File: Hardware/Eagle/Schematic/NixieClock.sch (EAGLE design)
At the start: 10 parts

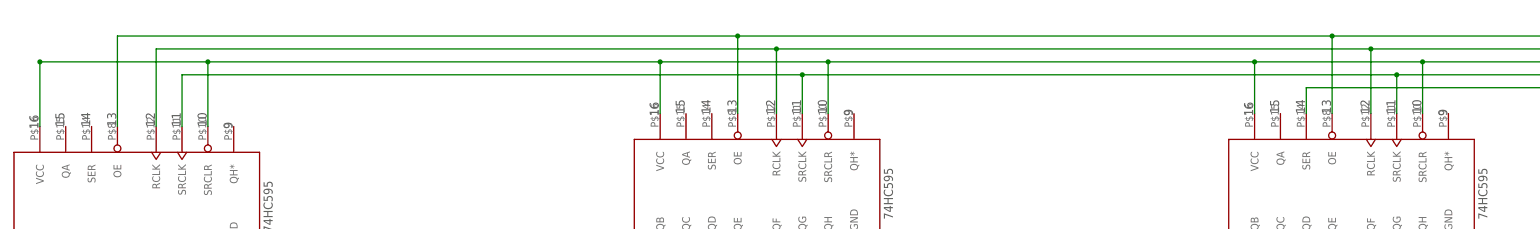
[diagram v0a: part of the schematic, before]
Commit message: Schematic progress... chips in board layout are out of order.. fix later
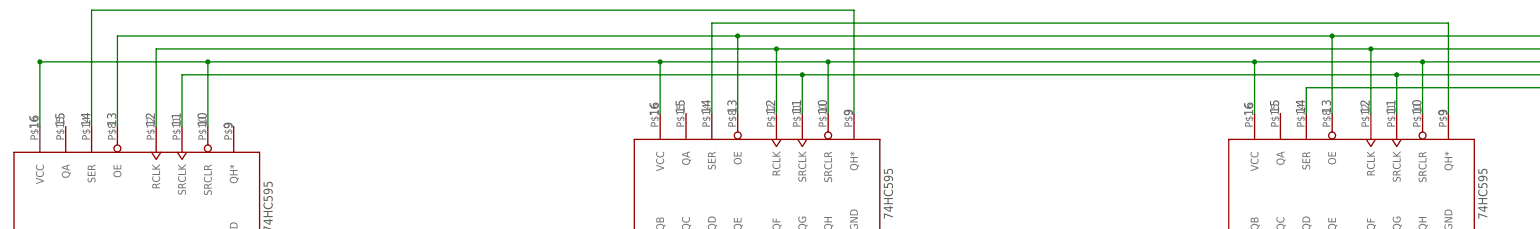
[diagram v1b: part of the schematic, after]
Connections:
- new net N$7: U$2.QH*, U$3.SER
- new net N$9: U$3.QH*, U$4.SER
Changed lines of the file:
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@@
+</segment>
+</net>
+<net name="N$7" class="0">
+<segment>
+<pinref part="U$2" gate="G$1" pin="QH*"/>
+<wire x1="124.46" y1="48.26" x2="124.46" y2="66.04" width="0.1524" layer="91"/>
+<pinref part="U$3" gate="G$1" pin="SER"/>
+<wire x1="124.46" y1="66.04" x2="-20.32" y2="66.04" width="0.1524" layer="91"/>
+<wire x1="-20.32" y1="66.04" x2="-20.32" y2="48.26" width="0.1524" layer="91"/>
+</segment>
+</net>
+<net name="N$9" class="0">
+<segment>
+<pinref part="U$3" gate="G$1" pin="QH*"/>
+<wire x1="7.62" y1="48.26" x2="7.62" y2="68.58" width="0.1524" layer="91"/>
+<pinref part="U$4" gate="G$1" pin="SER"/>
+<wire x1="7.62" y1="68.58" x2="-142.24" y2="68.58" width="0.1524" layer="91"/>
+<wire x1="-142.24" y1="68.58" x2="-142.24" y2="45.72" width="0.1524" layer="91"/>
 </segment>
 </net>

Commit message: All wires from shift registers to nixie driver inputs routed
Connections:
- new net N$10: U$10.IN_A, U$2.QH
- new net N$11: U$3.QH, U$8.IN_A
- new net N$12: U$4.QH, U$6.IN_A
- new net N$13: U$10.IN_B, U$2.QG
- new net N$14: U$3.QG, U$8.IN_B
- new net N$15: U$4.QG, U$6.IN_B
- new net N$16: U$10.IN_C, U$2.QF
- new net N$17: U$3.QF, U$8.IN_C
- new net N$18: U$4.QF, U$6.IN_C
- new net N$19: U$10.IN_D, U$2.QE
- new net N$20: U$3.QE, U$8.IN_D
- new net N$21: U$4.QE, U$6.IN_D
- new net N$22: U$2.QD, U$9.IN_A
- new net N$23: U$3.QD, U$7.IN_A
- new net N$24: U$4.QD, U$5.IN_A
- new net N$25: U$2.QC, U$9.IN_B
- new net N$26: U$3.QC, U$7.IN_B
- new net N$27: U$4.QC, U$5.IN_B
- new net N$28: U$2.QB, U$9.IN_C
- new net N$29: U$3.QB, U$7.IN_C
- new net N$30: U$4.QB, U$5.IN_C
- new net N$31: U$4.QA, U$5.IN_D
- new net N$32: U$3.QA, U$7.IN_D

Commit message: Molex connectors in place.. use part 39-30-6147 on mouser
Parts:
- added X1, X2, X3, X4, X5, X6: 5566-14, con-molex:5566-14

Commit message: Replaced 14 pin connector with 12 pin... started routing
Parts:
- removed X2, X3, X4, X5, X6: 5566-14, con-molex:5566-14
- added X7: 5566-12, con-molex:5566-12
- X1: value 5566-14 -> 5566-12; device con-molex:5566-14 -> con-molex:5566-12
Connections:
- new net N$33: U$5.OUT_0, X7-1.S
- new net N$34: U$5.OUT_1, X7-2.S
- new net N$35: U$5.OUT_2, X7-3.S
- new net N$36: U$5.OUT_4, X7-5.S
- new net N$37: U$5.OUT_5, X7-6.S
- new net N$38: U$5.OUT_6, X7-7.S
- new net N$39: U$5.OUT_7, X7-8.S
- new net N$40: U$5.OUT_3, X7-4.S
- new net N$41: U$5.OUT_8, X7-9.S
- new net N$42: U$5.OUT_9, X7-10.S
- new net N$43: U$10.OUT_0, X1-1.S
- new net N$44: U$10.OUT_1, X1-2.S
- new net N$45: X1-3.S
- new net N$46: U$10.OUT_6, X1-7.S
- new net N$47: U$10.OUT_7, X1-8.S
- new net N$48: U$10.OUT_3, X1-4.S
- new net N$49: U$10.OUT_4, X1-5.S
- new net N$50: U$10.OUT_5, X1-6.S
- new net N$51: X1-9.S
- new net N$52: X1-10.S
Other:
- moved on the sheet: X1-1, X1-10, X1-11, X1-12, X1-2, X1-3, X1-4, X1-5, X1-6, X1-7, X1-8, X1-9
